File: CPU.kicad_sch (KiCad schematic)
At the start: 208 parts, among them J1 Conn_02x36_Odd_Even, P10 Conn_02x08_Counter_Clockwise, P2 Conn_02x13_Top_Bottom, P3 Conn_02x13_Top_Bottom, P4 Conn_02x08_Counter_Clockwise, P5 Conn_02x25_Counter_Clockwise, P6 Conn_02x25_Counter_Clockwise, P7 Conn_02x07_Counter_Clockwise, P8 Conn_02x08_Counter_Clockwise

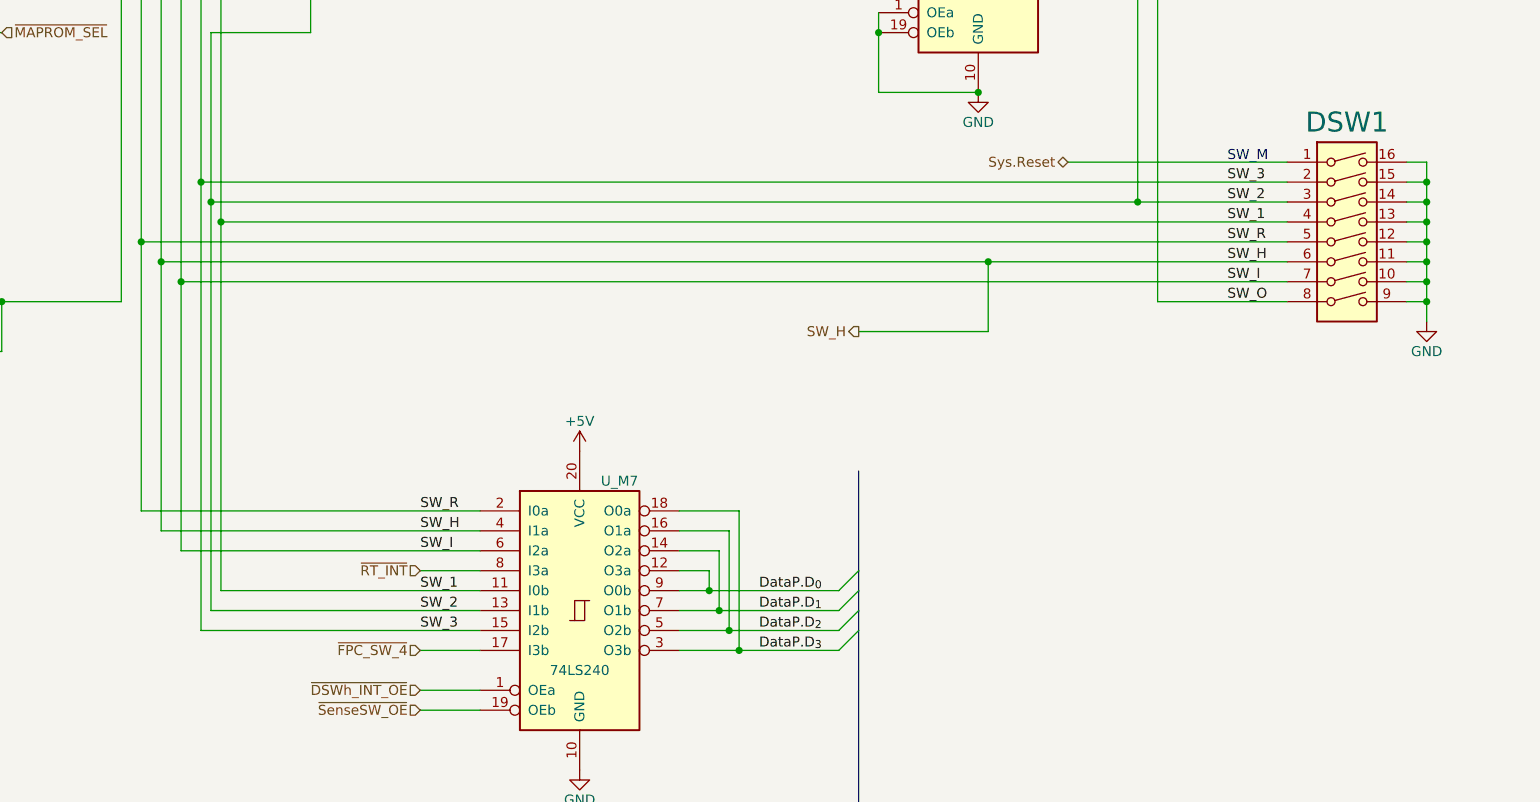
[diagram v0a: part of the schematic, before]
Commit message: Changed U_M7 pin assignments
Now lays out straight
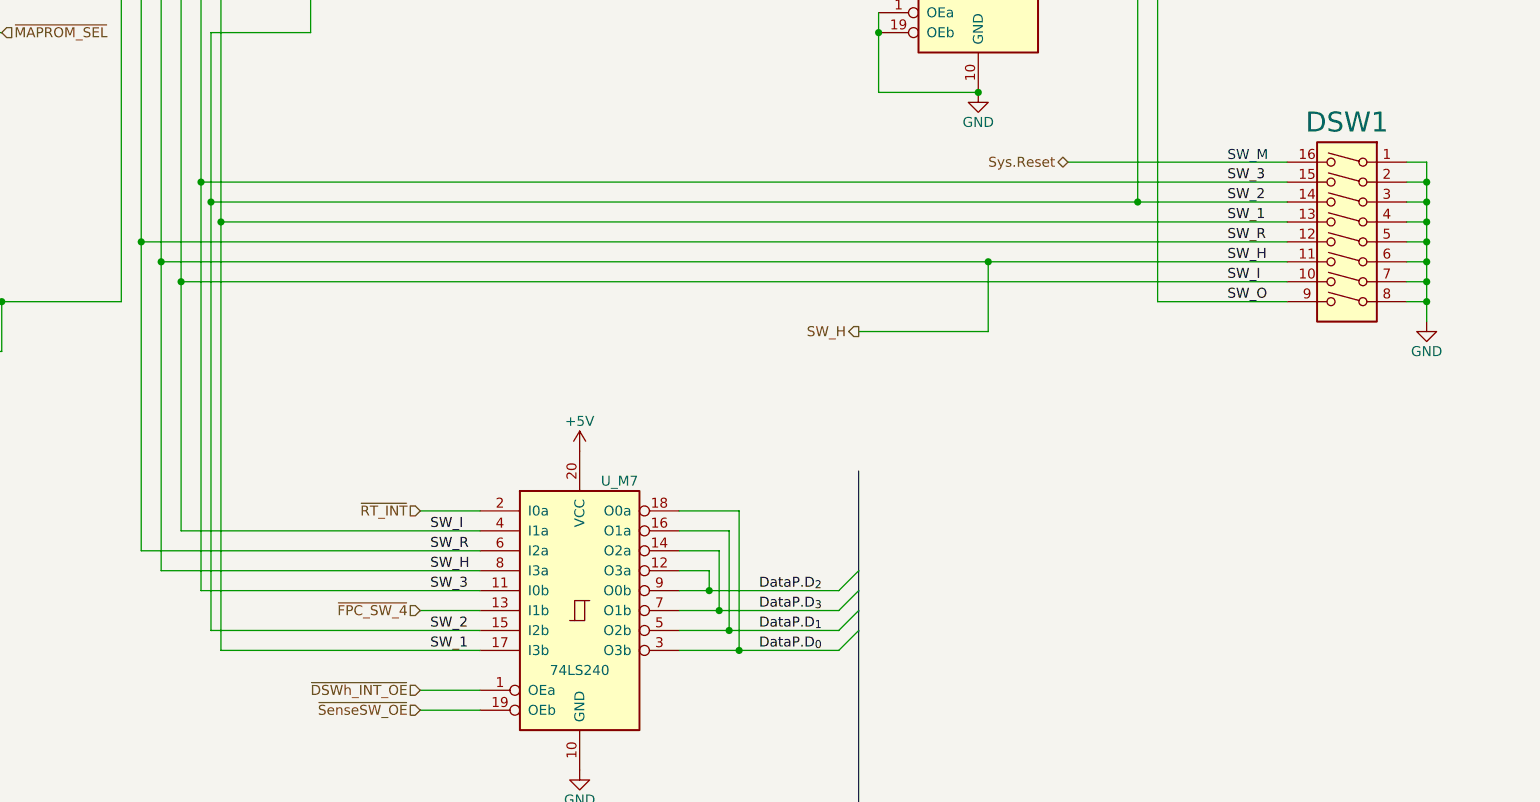
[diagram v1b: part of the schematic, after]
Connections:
- net DataP.D_{0}: now also U_M7.18 (O0a), U_M7.3 (O3b); no longer U_M7.12 (O3a), U_M7.9 (O0b)
- net DataP.D_{1}: now also U_M7.16 (O1a), U_M7.5 (O2b); no longer U_M7.14 (O2a), U_M7.7 (O1b)
- net DataP.D_{2}: now also U_M7.12 (O3a), U_M7.9 (O0b); no longer U_M7.16 (O1a), U_M7.5 (O2b)
- net DataP.D_{3}: now also U_M7.14 (O2a), U_M7.7 (O1b); no longer U_M7.18 (O0a), U_M7.3 (O3b)
- net GND: now also DSW1.1, DSW1.2, DSW1.3, DSW1.4, DSW1.5, DSW1.6, DSW1.7, DSW1.8; no longer DSW1.10, DSW1.11, DSW1.12, DSW1.13, DSW1.14, DSW1.15, DSW1.16, DSW1.9
- net SW_1: now also DSW1.13, U_M7.17 (I3b); no longer DSW1.4, U_M7.11 (I0b)
- net SW_2: now also DSW1.14, U_M7.15 (I2b); no longer DSW1.3, U_M7.13 (I1b)
- net SW_3: now also DSW1.15, U_M7.11 (I0b); no longer DSW1.2, U_M7.15 (I2b)
- net SW_H: now also DSW1.11, U_M7.8 (I3a); no longer DSW1.6, U_M7.4 (I1a)
- net SW_I: now also DSW1.10, U_M7.4 (I1a); no longer DSW1.7, U_M7.6 (I2a)
- net SW_O: now also DSW1.9; no longer DSW1.8
- net SW_R: now also DSW1.12, U_M7.6 (I2a); no longer DSW1.5, U_M7.2 (I0a)
- net Sys.Reset: now also DSW1.16; no longer DSW1.1
- net ~{FPC_SW_4}: now also U_M7.13 (I1b); no longer U_M7.17 (I3b)
- net ~{RT_INT}: now also U_M7.2 (I0a); no longer U_M7.8 (I3a)

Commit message: Change footprint on sense switch
Piano-style switch is better; that's why i swapped pins
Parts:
- DSW1: footprint Button_Switch_THT:SW_DIP_SPSTx08_Slide_9.78x22.5mm_W7.62mm_P2.54mm -> Button_Switch_THT:SW_DIP_SPSTx08_Piano_10.8x21.88mm_W7.62mm_P2.54mm
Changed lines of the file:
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@@
       (effects (font (size 1.27 1.27)) hide)
     )
-    (property "Footprint" "Button_Switch_THT:SW_DIP_SPSTx08_Slide_9.78x22.5mm_W7.62mm_P2.54mm" (id 2) (at 1102.36 486.41 0)
+    (property "Footprint" "Button_Switch_THT:SW_DIP_SPSTx08_Piano_10.8x21.88mm_W7.62mm_P2.54mm" (id 2) (at 1102.36 486.41 0)
       (effects (font (size 1.27 1.27)) hide)
     )
@@
     )
     (path "/0e0f6599-d617-4724-a56a-b1f9871a19f6"
-      (reference "DSW1") (unit 1) (value "SW_DIP_x08") (footprint "Button_Switch_THT:SW_DIP_SPSTx08_Slide_9.78x22.5mm_W7.62mm_P2.54mm")
+      (reference "DSW1") (unit 1) (value "SW_DIP_x08") (footprint "Button_Switch_THT:SW_DIP_SPSTx08_Piano_10.8x21.88mm_W7.62mm_P2.54mm")
     )
     (path "/204a5142-3c33-4dca-b85e-682e0b14a381"

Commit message: Optimized connections around R7
Removed debugging connections, switched pins around for straight tracks.
Some inverters optimized away due to debug harness removal
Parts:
- removed R7: 4.7k, Resistor_THT:R_Array_SIP10, symbol Device:R_Network09
- added R7: 4.7K, Resistor_THT:R_Array_SIP9, symbol Device:R_Network08
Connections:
- net +5V: now also R7.1 (common)
- net GND: now also U_J6.11, U_J7.22 (~{OE}), U_K7.22 (~{OE}), U_L9.22 (~{OE})
- net P7_3: no longer U_J6.11
- net SW_1: now also R7.4 (R3)
- net SW_3: now also R7.3 (R2)
- net SW_H: now also R7.6 (R5)
- net SW_I: now also R7.7 (R6)
- net SW_R: now also R7.5 (R4)
- net ~{MAPROM_SEL}: now also U_L6.9
- net at P2.13 (Pin_13): now also R7.8 (R7)
- net P7_9: no longer names the net of P7.9 (Pin_9)
- net P7_9: no longer U_L6.9
- removed net SEQ.~{OE}: U_J6.10, U_J7.22 (~{OE}), U_K7.22 (~{OE}), U_L9.22 (~{OE})
- no-connect marks 92 -> 95
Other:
- moved on the sheet: U_J6E, U_L6C

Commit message: Smaller footprints
Chanded C39 and XTAL to smaller footprints
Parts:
- C39: footprint Capacitor_THT:CP_Axial_L18.0mm_D8.0mm_P25.00mm_Horizontal -> Capacitor_THT:CP_Radial_D8.0mm_P3.50mm
- XTAL1: footprint Crystal:Crystal_HC52-U_Horizontal -> Crystal:Crystal_HC18-U_Vertical
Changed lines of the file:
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@@
     (property "Reference" "XTAL1" (id 0) (at 904.24 298.45 0))
     (property "Value" "15.000MHz" (id 1) (at 904.24 300.99 0))
-    (property "Footprint" "Crystal:Crystal_HC52-U_Horizontal" (id 2) (at 904.24 306.07 0)
+    (property "Footprint" "Crystal:Crystal_HC18-U_Vertical" (id 2) (at 904.24 306.07 0)
       (effects (font (size 1.27 1.27)) hide)
     )
@@
       (effects (font (size 1.27 1.27)) (justify left))
     )
-    (property "Footprint" "Capacitor_THT:CP_Axial_L18.0mm_D8.0mm_P25.00mm_Horizontal" (id 2) (at 116.5352 170.18 0)
+    (property "Footprint" "Capacitor_THT:CP_Radial_D8.0mm_P3.50mm" (id 2) (at 116.5352 170.18 0)
       (effects (font (size 1.27 1.27)) hide)
     )
@@
     )
     (path "/9af04a29-a43b-4697-8379-18fe5ce3a759"
-      (reference "C39") (unit 1) (value "470uF") (footprint "Capacitor_THT:CP_Axial_L18.0mm_D8.0mm_P25.00mm_Horizontal")
+      (reference "C39") (unit 1) (value "470uF") (footprint "Capacitor_THT:CP_Radial_D8.0mm_P3.50mm")
     )
     (path "/a92a0c0c-b153-4b77-8748-30093508820c"
@@
     )
     (path "/062033f7-deb0-4cd0-a29c-ab8812e00794"
-      (reference "XTAL1") (unit 1) (value "15.000MHz") (footprint "Crystal:Crystal_HC52-U_Horizontal")
+      (reference "XTAL1") (unit 1) (value "15.000MHz") (footprint "Crystal:Crystal_HC18-U_Vertical")
     )
   )
